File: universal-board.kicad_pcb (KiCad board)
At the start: 2 copper layers, 61.2 x 77.5 mm, 52 parts, among them J1 USB_C_Receptacle, J2 CONN_I2C_GROVE, J4 CONN_CC1101_2, J5 CONN_CC1101_1, J6 CONN_UART, J7 CONN_WS2812, Q1 BSS138, U1 ESP32-S2-MINI-2, U2 AMS1117-3.3, U3 TSOP384xx, U4 74AHCT1G125

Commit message: Further minor changes to make DRC happy.
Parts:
- moved R3 4.76 mm to (72.8, 82.0), turned to 90 degrees
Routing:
- net 5V: track 62.0 -> 114.5 mm, vias 0 -> 1
- net SW_ACK_OUT: track 19.7 -> 26.2 mm
- net Net-(SW1-B): track 10.8 -> 17.3 mm
- net GND: track 251.4 -> 248.1 mm
- net 3.3V: track 147.5 -> 146.6 mm
- net Net-(J1-CC2): track 8.36 -> 8.98 mm
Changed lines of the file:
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@@
 	(footprint "Resistor_SMD:R_1206_3216Metric_Pad1.30x1.75mm_HandSolder"
 		(layer "F.Cu")
-		(at 71.2 77.5 -90)
+		(at 72.75 82 90)
 		(descr "Resistor SMD 1206 (3216 Metric), square (rectangular) end terminal, IPC-7351 nominal with elongated pad for handsoldering. (Body size source: IPC-SM-782 page 72, https://www.pcb-3d.com/wordpress/wp-content/uploads/ipc-sm-782a_amendment_1_and_2.pdf), generated with kicad-footprint-generator")
 		(tags "resistor handsolder")
@@
 		(attr smd)
 		(fp_line
-			(start -0.727064 0.91)
-			(end 0.727064 0.91)
+			(start -0.727064 -0.91)
+			(end 0.727064 -0.91)
 			(stroke
 				(width 0.12)
@@
 		)
 		(fp_line
-			(start -0.727064 -0.91)
-			(end 0.727064 -0.91)
+			(start -0.727064 0.91)
+			(end 0.727064 0.91)
 			(stroke
 				(width 0.12)
@@
 		)
 		(pad "1" smd roundrect
-			(at -1.55 0 270)
+			(at -1.55 0 90)
 			(size 1.3 1.75)
 			(layers "F.Cu" "F.Mask" "F.Paste")
@@
 		)
 		(pad "2" smd roundrect
-			(at 1.55 0 270)
+			(at 1.55 0 90)
 			(size 1.3 1.75)
 			(layers "F.Cu" "F.Mask" "F.Paste")
@@
 	)
 	(segment
-		(start 71.2 76.1)
-		(end 73.48 73.82)
-		(width 0.2)
-		(layer "F.Cu")
-		(net 1)
-	)
-	(segment
 		(start 74.08 77.925)
 		(end 73.48 77.325)
@@
 	)
 	(segment
-		(start 71.2 76.15)
-		(end 71.2 76.1)
-		(width 0.2)
-		(layer "F.Cu")
-		(net 1)
-	)
-	(segment
 		(start 111.599 145.201)
 		(end 86 145.201)
@@
 	)
 	(segment
+		(start 104.3375 77.8375)
+		(end 104.3375 79.8)
+		(width 0.2)
+		(layer "F.Cu")
+		(net 3)
+	)
+	(segment
 		(start 86 86.3)
 		(end 87.7 84.6)
@@
 	)
 	(segment
+		(start 104.25 77.75)
+		(end 104.3375 77.8375)
+		(width 0.2)
+		(layer "F.Cu")
+		(net 3)
+	)
+	(segment
 		(start 85.9625 88.8)
 		(end 85.9625 91.1625)
@@
 		(net 3)
 	)
+	(via
+		(at 104.25 77.75)
+		(size 0.6)
+		(drill 0.3)
+		(layers "F.Cu" "B.Cu")
+		(net 3)
+	)
+	(segment
+		(start 105.321 119.701)
+		(end 110.648943 119.701)
+		(width 0.2)
+		(layer "B.Cu")
+		(net 3)
+	)
+	(segment
+		(start 110.648943 119.701)
+		(end 111.001 119.348943)
+		(width 0.2)
+		(layer "B.Cu")
+		(net 3)
+	)
+	(segment
+		(start 111.001 119.348943)
+		(end 111.001 117.9681)
+		(width 0.2)
+		(layer "B.Cu")
+		(net 3)
+	)
+	(segment
+		(start 111.001 117.9681)
+		(end 107.201 114.1681)
+		(width 0.2)
+		(layer "B.Cu")
+		(net 3)
+	)
+	(segment
+		(start 105.2 119.58)
+		(end 105.321 119.701)
+		(width 0.2)
+		(layer "B.Cu")
+		(net 3)
+	)
+	(segment
+		(start 107.201 114.1681)
+		(end 107.201 80.701)
+		(width 0.2)
+		(layer "B.Cu")
+		(net 3)
+	)
+	(segment
+		(start 107.201 80.701)
+		(end 104.25 77.75)
+		(width 0.2)
+		(layer "B.Cu")
+		(net 3)
+	)
 	(segment
 		(start 109.9 140.5)
@@
 	)
 	(segment
-		(start 95.3625 93.5)
-		(end 95.3625 92.5875)
-		(width 0.2)
-		(layer "F.Cu")
-		(net 4)
-	)
-	(segment
 		(start 112.1 118.5)
 		(end 113.35 118.5)
@@
 	)
 	(segment
-		(start 71.2 77.922215)
-		(end 71.2 79.25)
+		(start 73.148215 75.974)
+		(end 72.679 76.443215)
 		(width 0.2)
 		(layer "F.Cu")
@@
 	)
 	(segment
-		(start 73.148215 75.974)
-		(end 71.2 77.922215)
+		(start 72.679 76.443215)
+		(end 72.679 80.379)
 		(width 0.2)
 		(layer "F.Cu")
@@
 	)
 	(segment
+		(start 72.679 80.379)
+		(end 72.75 80.45)
+		(width 0.2)
+		(layer "F.Cu")
+		(net 15)
+	)
+	(segment
 		(start 75.069 75.974)
 		(end 73.148215 75.974)
@@
 	)
 	(segment
+		(start 115.85 125.85)
+		(end 109.35 125.85)
+		(width 0.2)
+		(layer "B.Cu")
+		(net 30)
+	)
+	(segment
 		(start 110.651 119.351)
 		(end 110.4 119.1)
@@
 	)
 	(segment
+		(start 109.35 129.25)
+		(end 115.85 129.25)
+		(width 0.2)
+		(layer "B.Cu")
+		(net 31)
+	)
+	(segment
 		(start 87.09 104.575)
 		(end 87.675 104.575)
@@
 				(xy 114.3 139.45) (xy 114 139.45) (xy 113.8 139.65) (xy 113.8 146.4) (xy 82 146.4) (xy 75.8 140.2)
 				(xy 75.8 138.4) (xy 73.4 136) (xy 66.45 136) (xy 66.35 136.1) (xy 66.25 136) (xy 66.25 130) (xy 86.2 130)
-				(xy 86.2 111) (xy 80 104.8) (xy 80 90.9) (xy 80.3 90.6) (xy 80.3 89.1) (xy 71.2 80)
+				(xy 86.2 111) (xy 80 104.8) (xy 80 92) (xy 79.05 92) (xy 71.2 84)
 			)
 		)

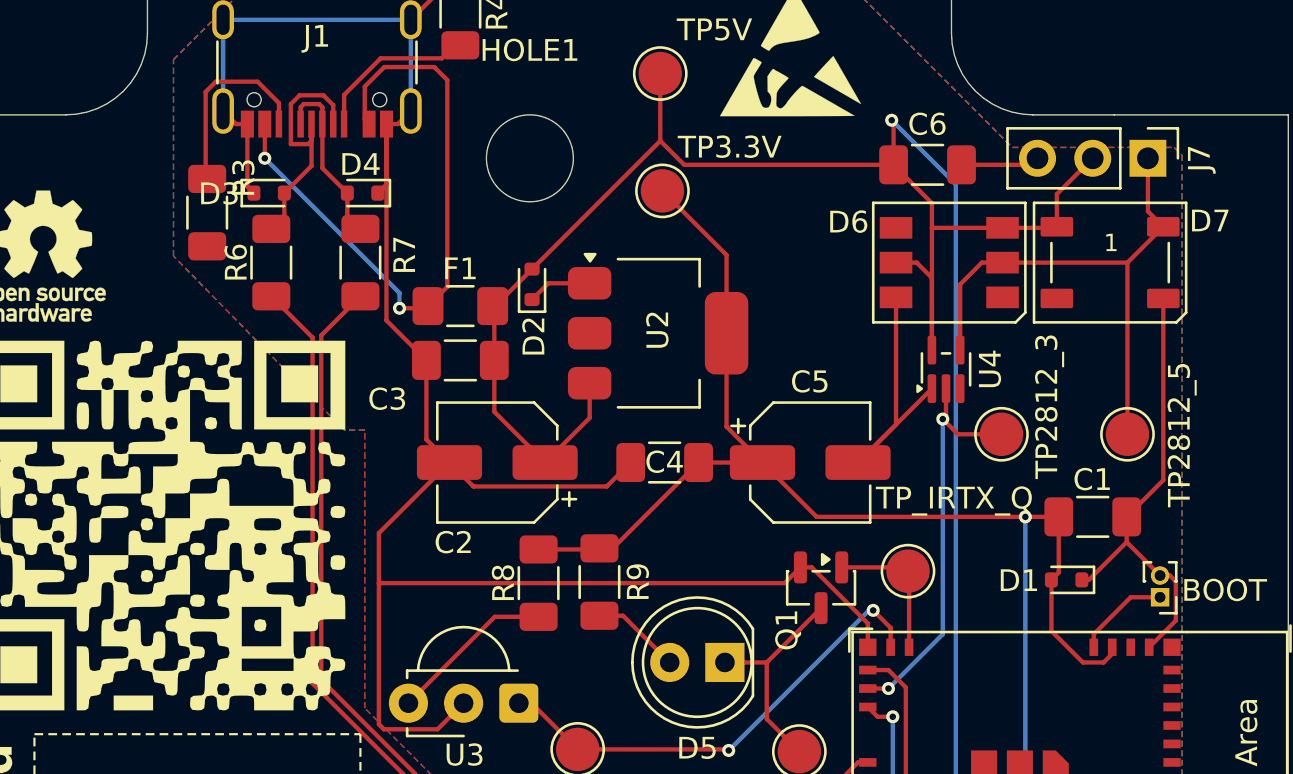
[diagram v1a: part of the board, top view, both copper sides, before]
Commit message: Changed TVS diodes to ElecSuper PESD5V0L1BA,115-ES (bigger, easier to solder).
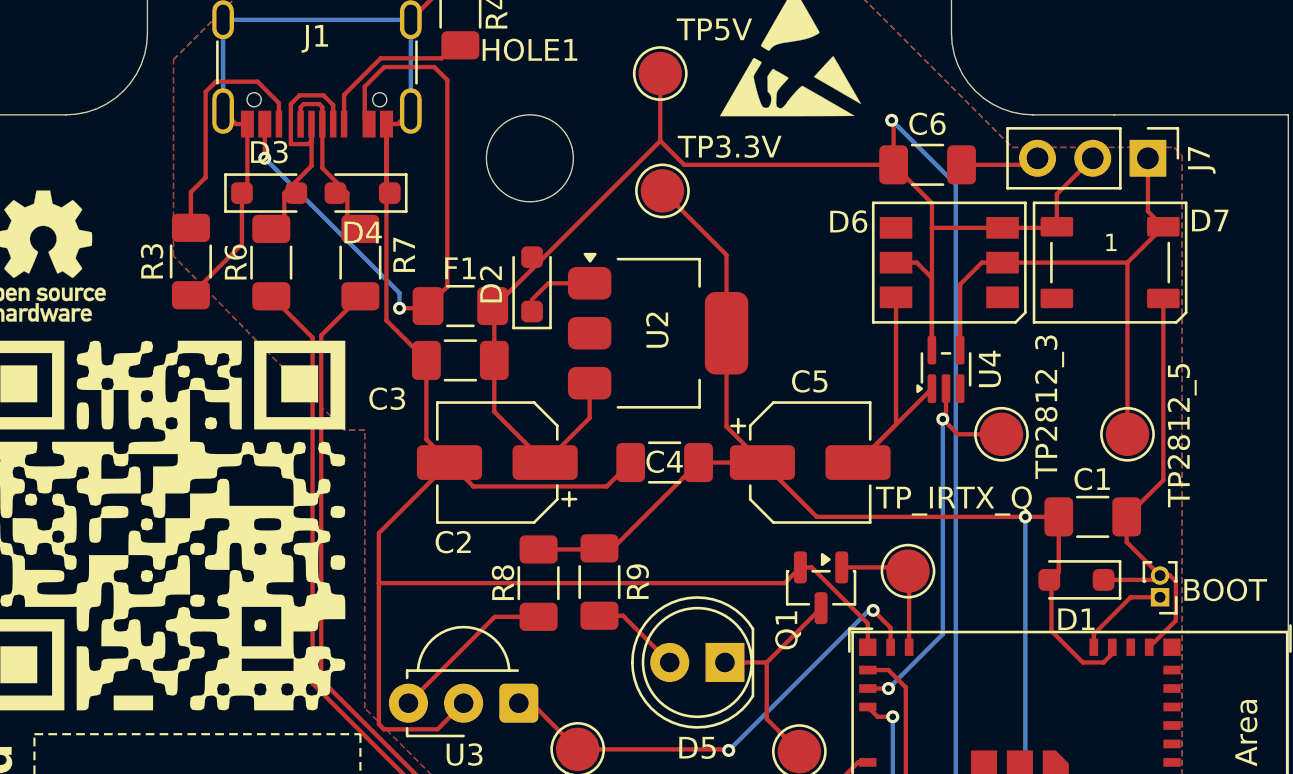
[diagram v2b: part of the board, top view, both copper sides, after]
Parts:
- D1, D2, D3, D4: value LESD5D5.0CT1G -> PESD5V0L1BA,115-ES; footprint Diode_SMD:D_SOD-523 -> Diode_SMD:D_SOD-323_HandSoldering
- moved R3 2.37 mm to (72.0, 84.2)
- moved D1 0.45 mm to (112.8, 98.9)
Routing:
- net GND: track 248.1 -> 252.7 mm
- net Net-(J1-CC2): track 8.98 -> 11.5 mm
- net 3.3V: track 146.6 -> 147.1 mm
